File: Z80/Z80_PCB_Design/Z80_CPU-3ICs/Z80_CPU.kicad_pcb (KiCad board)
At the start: 2 copper layers, 95 x 95 mm, 36 parts, among them J1 Conn_01x04, J5 Conn_01x04, J6 USB_B, U1 Z80CPU, U10 4.9152 MHz, U2 AS6C4008-55PCN, U8 CY8C5267AXI-LP051, Y1 32.768KHz

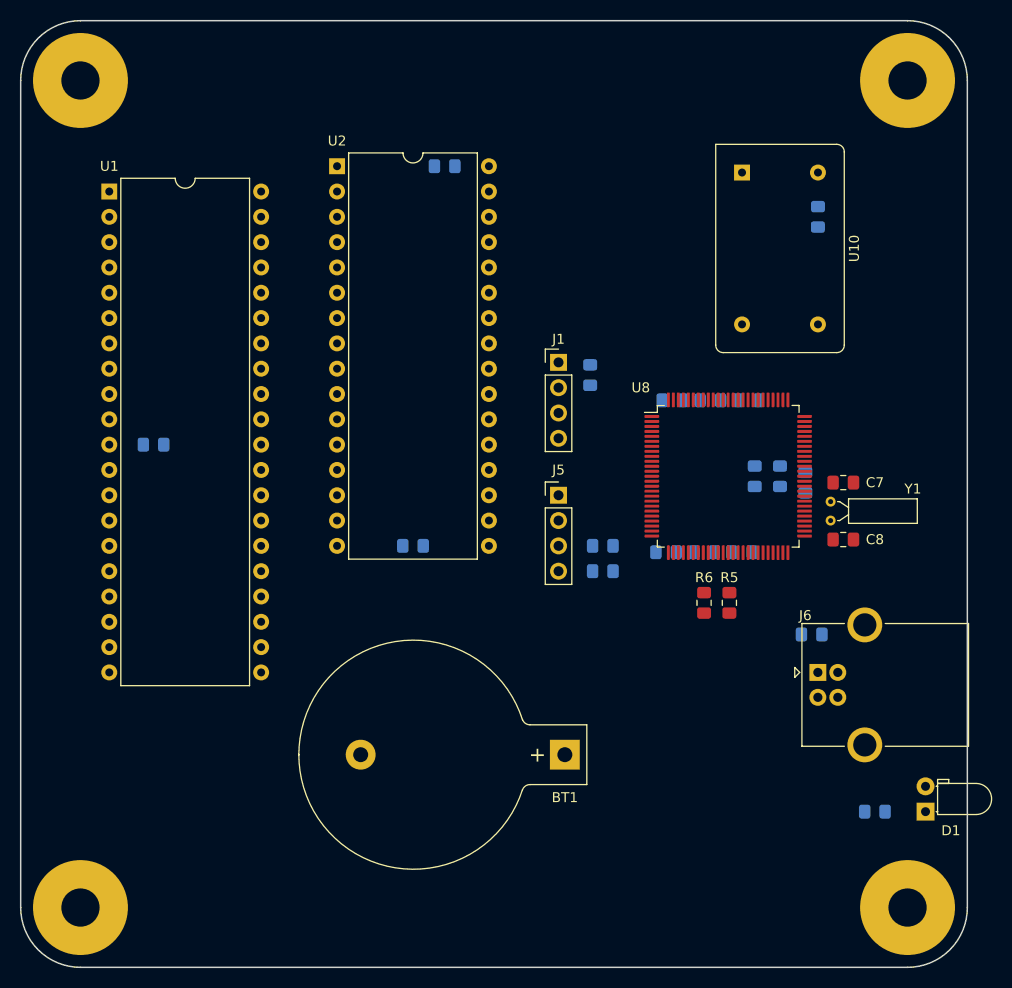
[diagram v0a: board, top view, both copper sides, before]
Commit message: Z80 3-chip Single Board Computer
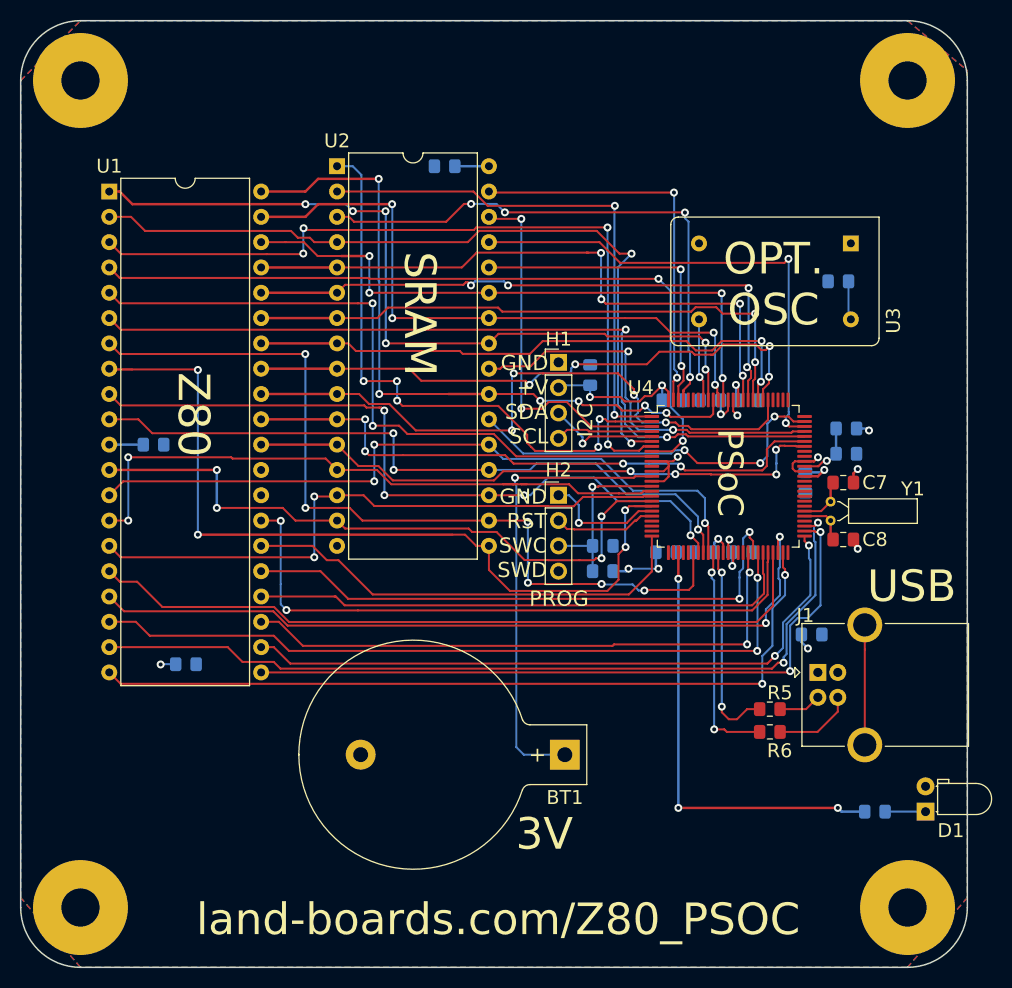
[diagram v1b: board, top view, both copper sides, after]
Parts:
- moved C6 25.7 mm to (16.6, 64.6), turned to 180 degrees
- moved R6 14.5 mm to (75.2, 71.4), turned to 180 degrees
- moved U3 13.0 mm to (83.3, 22.4), turned to 180 degrees
- moved R5 11.4 mm to (75.2, 69.1), turned to 180 degrees
- moved C4 9.47 mm to (82.9, 43.5), turned to 0 degrees
- moved L1 8.20 mm to (82.9, 40.9), turned to 0 degrees
- moved C14 6.79 mm to (82.1, 26.2), turned to 0 degrees
- renumbered J1 to H1, J5 to H2, J6 to J1, U10 to U3, U8 to U4
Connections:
- H1 pad 3: /SCL -> /SDA
- H1 pad 4: /SDA -> /SCL
- U4 pad 25: (no net) -> /~CPURST
- U4 pad 42: (no net) -> /~BUSACK
- U4 pad 43: (no net) -> /~BUSRQ
- U4 pad 44: /CPUCLK -> /~HALT
- U4 pad 45: /~MEMRD -> /~WAIT
- U4 pad 46: /~MEMWR -> /~M1
- U4 pad 47: /~SRAMCS -> /~INT
- U4 pad 48: /~IORQ -> /~NMI
- U4 pad 49: /~CPUWR -> /~IORQ
- U4 pad 51: /~CPURD -> /~CPUWR
- U4 pad 52: /~MREQ -> /~CPURD
- U4 pad 53: (no net) -> /~MREQ
- U4 pad 71: /~BUSACK -> /CPUCLK
- U4 pad 72: /~BUSRQ -> /~MEMRD
- U4 pad 73: /~HALT -> /~MEMWR
- U4 pad 74: /~WAIT -> /~SRAMCS
- U4 pad 76: /~M1 -> (no net)
- U4 pad 77: /~INT -> (no net)
- U4 pad 78: /~NMI -> (no net)
- U4 pad 79: /~CPURST -> (no net)
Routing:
- net /~MREQ: track 0.00 -> 85.9 mm, vias 0 -> 2
- net /CPUD4: track 0.00 -> 85.0 mm, vias 0 -> 6
- net /CPUD3: track 0.00 -> 83.8 mm, vias 0 -> 4
- net /CPUCLK: track 0.00 -> 80.8 mm, vias 0 -> 2
- net /CPUA11: track 0.00 -> 80.5 mm, vias 0 -> 6
- net /~IORQ: track 0.00 -> 80.2 mm, vias 0 -> 2
- net /CPUA13: track 0.00 -> 79.9 mm, vias 0 -> 4
- net /~NMI: track 0.00 -> 78.3 mm, vias 0 -> 2
- net /CPUA12: track 0.00 -> 77.2 mm, vias 0 -> 2
- net /CPUA14: track 0.00 -> 76.4 mm, vias 0 -> 2
- net /~HALT: track 0.00 -> 76.1 mm, vias 0 -> 2
- net /~INT: track 0.00 -> 74.7 mm
- net /CPUD5: track 0.00 -> 73.5 mm, vias 0 -> 4
- net /CPUD7: track 0.00 -> 71.9 mm, vias 0 -> 3
- net /~CPURD: track 0.00 -> 70.6 mm, vias 0 -> 2
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- added copper zone on F.Cu, net +5V
- added copper zone on B.Cu, net GND
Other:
- net class Default: clearance 0.2 -> 0.1524; trace_width 0.25 -> 0.2032
- rule trace_clearance: 0.2 -> 0.1524
- board text added: "3V"
- board text added: "GND +V SDA SCL"
- board text added: "GND RST SWC SWD"
- board text added: "I2C"
- board text added: "OPT. OSC"
- board text added: "PROG"
- board text added: "PSoC"
- board text added: "SRAM"
- board text added: "USB"
- board text added: "Z80"
- board text added: "land-boards.com/Z80_PSOC"

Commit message: Z80 layout
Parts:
- added H3: Conn_01x06, Connector_PinHeader_2.54mm:PinHeader_1x06_P2.54mm_Vertical, F.Cu at (91.7, 24.5)
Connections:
- net Net-(H2-Pad1) renamed /SWD
- net Net-(H2-Pad2) renamed /SWC
- U4 pad 76: (no net) -> /P76
- U4 pad 77: (no net) -> /P77
- U4 pad 78: (no net) -> /P78
- U4 pad 79: (no net) -> /P79
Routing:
- net /P79: track 0.00 -> 23.2 mm, vias 0 -> 2
- net /P78: track 0.00 -> 21.2 mm, vias 0 -> 2
- net /P77: track 0.00 -> 17.0 mm, vias 0 -> 2
- net /P76: track 0.00 -> 15.1 mm, vias 0 -> 2
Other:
- board text added: "GND +V P79 P78 P77 P76"
